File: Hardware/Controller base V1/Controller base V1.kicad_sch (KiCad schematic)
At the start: 30 parts, among them J1 USB_C_Receptacle_USB2.0_16P, J2 Conn_01x05_Pin, J7 Conn_02x10_Counter_Clockwise, J8 Conn_02x10_Counter_Clockwise, SW4 SW_Push, U1 AZ1117CH-3.3TRG1, U2 ESP32-S3-WROOM-1U-N4

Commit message: update
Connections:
- net GND: no longer J8.16, J8.18
- net GPIO39: now reaches U2.32 (IO39)
- net GPIO39: now also J8.16
- net GPIO40: now reaches U2.33 (IO40)
- net GPIO40: now also J8.18
- no-connect marks 6 -> 4
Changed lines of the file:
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@@
 	)
 	(junction
-		(at 271.78 91.44)
-		(diameter 0)
-		(color 0 0 0 0)
-	)
-	(junction
 		(at 157.48 31.75)
 		(diameter 0)
@@
 	)
 	(no_connect
-		(at 209.55 127)
-	)
-	(no_connect
 		(at 48.26 64.77)
 	)
 	(no_connect
-		(at 209.55 129.54)
-	)
-	(no_connect
 		(at 48.26 62.23)
 	)
@@
 	(wire
 		(pts
-			(xy 21.59 163.83) (xy 29.21 163.83)
+			(xy 271.78 97.79) (xy 271.78 93.98)
 		)
 		(stroke
@@
 	(wire
 		(pts
-			(xy 102.87 31.75) (xy 115.57 31.75)
+			(xy 209.55 127) (xy 210.82 127)
 		)
 		(stroke
@@
 	(wire
 		(pts
-			(xy 210.82 132.08) (xy 209.55 132.08)
+			(xy 21.59 163.83) (xy 29.21 163.83)
 		)
 		(stroke
@@
 	(wire
 		(pts
-			(xy 154.94 152.4) (xy 154.94 144.78)
+			(xy 102.87 31.75) (xy 115.57 31.75)
 		)
 		(stroke
@@
 	(wire
 		(pts
-			(xy 176.53 134.62) (xy 179.07 134.62)
+			(xy 210.82 132.08) (xy 209.55 132.08)
 		)
 		(stroke
@@
 	(wire
 		(pts
-			(xy 81.28 189.23) (xy 87.63 189.23)
+			(xy 154.94 152.4) (xy 154.94 144.78)
 		)
 		(stroke
@@
 	(wire
 		(pts
-			(xy 271.78 88.9) (xy 271.78 91.44)
+			(xy 176.53 134.62) (xy 179.07 134.62)
+		)
+		(stroke
+			(width 0)
+			(type default)
+		)
+	)
+	(wire
+		(pts
+			(xy 81.28 189.23) (xy 87.63 189.23)
 		)
 		(stroke
@@
 	(wire
 		(pts
-			(xy 271.78 91.44) (xy 276.86 91.44)
-		)
-		(stroke
-			(width 0)
-			(type default)
-		)
-	)
-	(wire
-		(pts
 			(xy 247.65 83.82) (xy 252.73 83.82)
 		)
@@
 	(wire
 		(pts
+			(xy 209.55 129.54) (xy 210.82 129.54)
+		)
+		(stroke
+			(width 0)
+			(type default)
+		)
+	)
+	(wire
+		(pts
 			(xy 153.67 87.63) (xy 153.67 88.9)
 		)
@@
 	(wire
 		(pts
-			(xy 271.78 93.98) (xy 271.78 91.44)
-		)
-		(stroke
-			(width 0)
-			(type default)
-		)
-	)
-	(wire
-		(pts
 			(xy 170.18 31.75) (xy 170.18 34.29)
 		)
@@
 	(wire
 		(pts
-			(xy 265.43 88.9) (xy 271.78 88.9)
+			(xy 247.65 76.2) (xy 252.73 76.2)
 		)
 		(stroke
@@
 	(wire
 		(pts
-			(xy 247.65 76.2) (xy 252.73 76.2)
+			(xy 210.82 144.78) (xy 209.55 144.78)
 		)
 		(stroke
@@
 	(wire
 		(pts
-			(xy 210.82 144.78) (xy 209.55 144.78)
+			(xy 67.31 49.53) (xy 67.31 57.15)
 		)
 		(stroke
@@
 	(wire
 		(pts
-			(xy 67.31 49.53) (xy 67.31 57.15)
+			(xy 55.88 85.09) (xy 49.53 85.09)
 		)
 		(stroke
@@
 	(wire
 		(pts
-			(xy 55.88 85.09) (xy 49.53 85.09)
+			(xy 271.78 59.69) (xy 271.78 57.15)
 		)
 		(stroke
@@
 	(wire
 		(pts
-			(xy 271.78 59.69) (xy 271.78 57.15)
+			(xy 74.93 52.07) (xy 72.39 52.07)
 		)
 		(stroke
@@
 	(wire
 		(pts
-			(xy 74.93 52.07) (xy 72.39 52.07)
+			(xy 67.31 46.99) (xy 48.26 46.99)
 		)
 		(stroke
@@
 	(wire
 		(pts
-			(xy 67.31 46.99) (xy 48.26 46.99)
+			(xy 265.43 91.44) (xy 271.78 91.44)
 		)
 		(stroke
@@
 	(wire
 		(pts
-			(xy 59.69 34.29) (xy 59.69 57.15)
+			(xy 265.43 88.9) (xy 271.78 88.9)
 		)
 		(stroke
@@
 	(wire
 		(pts
-			(xy 271.78 54.61) (xy 271.78 52.07)
+			(xy 59.69 34.29) (xy 59.69 57.15)
 		)
 		(stroke
@@
 	(wire
 		(pts
-			(xy 53.34 80.01) (xy 49.53 80.01)
+			(xy 271.78 54.61) (xy 271.78 52.07)
 		)
 		(stroke
@@
 	(wire
 		(pts
-			(xy 49.53 179.07) (xy 58.42 179.07)
+			(xy 53.34 80.01) (xy 49.53 80.01)
 		)
 		(stroke
@@
 	(wire
 		(pts
-			(xy 81.28 186.69) (xy 87.63 186.69)
+			(xy 49.53 179.07) (xy 58.42 179.07)
 		)
 		(stroke
@@
 	(wire
 		(pts
-			(xy 132.08 41.91) (xy 132.08 46.99)
+			(xy 81.28 186.69) (xy 87.63 186.69)
 		)
 		(stroke
@@
 	(wire
 		(pts
-			(xy 265.43 91.44) (xy 271.78 91.44)
+			(xy 132.08 41.91) (xy 132.08 46.99)
 		)
 		(stroke
@@
 		)
 	)
+	(global_label "GPIO40"
+		(shape input)
+		(at 271.78 91.44 0)
+		(fields_autoplaced yes)
+		(effects
+			(font
+				(size 1.27 1.27)
+			)
+			(justify left)
+		)
+		(property "Intersheetrefs" "${INTERSHEET_REFS}"
+			(at 281.6595 91.44 0)
+			(effects
+				(font
+					(size 1.27 1.27)
+				)
+				(justify left)
+				(hide yes)
+			)
+		)
+	)
 	(global_label "GPIO11"
 		(shape input)
@@
 		)
 	)
+	(global_label "GPIO39"
+		(shape input)
+		(at 210.82 127 0)
+		(fields_autoplaced yes)
+		(effects
+			(font
+				(size 1.27 1.27)
+			)
+			(justify left)
+		)
+		(property "Intersheetrefs" "${INTERSHEET_REFS}"
+			(at 220.6995 127 0)
+			(effects
+				(font
+					(size 1.27 1.27)
+				)
+				(justify left)
+				(hide yes)
+			)
+		)
+	)
 	(global_label "GPIO4"
 		(shape input)
@@
 		)
 	)
+	(global_label "GPIO39"
+		(shape input)
+		(at 271.78 88.9 0)
+		(fields_autoplaced yes)
+		(effects
+			(font
+				(size 1.27 1.27)
+			)
+			(justify left)
+		)
+		(property "Intersheetrefs" "${INTERSHEET_REFS}"
+			(at 281.6595 88.9 0)
+			(effects
+				(font
+					(size 1.27 1.27)
+				)
+				(justify left)
+				(hide yes)
+			)
+		)
+	)
 	(global_label "GPIO8"
 		(shape input)
@@
 		)
 	)
+	(global_label "GPIO40"
+		(shape input)
+		(at 210.82 129.54 0)
+		(fields_autoplaced yes)
+		(effects
+			(font
+				(size 1.27 1.27)
+			)
+			(justify left)
+		)
+		(property "Intersheetrefs" "${INTERSHEET_REFS}"
+			(at 220.6995 129.54 0)
+			(effects
+				(font
+					(size 1.27 1.27)
+				)
+				(justify left)
+				(hide yes)
+			)
+		)
+	)
 	(global_label "GPIO38"
 		(shape input)
@@
 	(symbol
 		(lib_id "MCU_Controller:GND")
-		(at 276.86 91.44 90)
+		(at 271.78 97.79 0)
 		(unit 1)
 		(exclude_from_sim no)
@@
 		(fields_autoplaced yes)
 		(property "Reference" "#PWR030"
-			(at 283.21 91.44 0)
+			(at 271.78 104.14 0)
 			(effects
 				(font
@@
 		)
 		(property "Value" "GND"
-			(at 280.67 91.4399 90)
+			(at 274.32 99.0599 0)
 			(effects
 				(font
 					(size 1.27 1.27)
 				)
-				(justify right)
+				(justify left)
 			)
 		)
 		(property "Footprint" ""
-			(at 276.86 91.44 0)
+			(at 271.78 97.79 0)
 			(effects
 				(font
@@
 		)
 		(property "Datasheet" ""
-			(at 276.86 91.44 0)
+			(at 271.78 97.79 0)
 			(effects
 				(font
@@
 		)
 		(property "Description" "Power symbol creates a global label with name \"GND\" , ground"
-			(at 276.86 91.44 0)
+			(at 271.78 97.79 0)
 			(effects
 				(font

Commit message: added test points
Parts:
- added 3V3, Gnd1, VBUS1: TestPoint, MCU_Controller:TestPoint_Pad_D1.0mm, symbol MCU_Controller:TestPoint
- renumbered TP4 to D+1, TP3 to D-1, J7 to J3, J8 to J4, TP1 to RX0, SW4 to SW1, TP2 to TX0
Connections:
- net GND: now also Gnd1.1
- net VBUS: now also VBUS1.1
- net VCC_3V3: now also 3V3.1

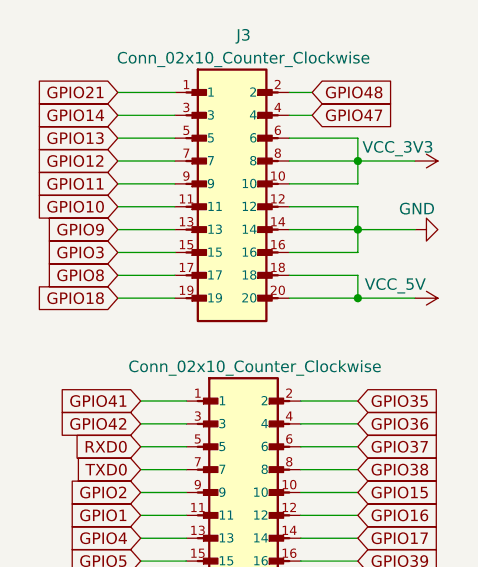
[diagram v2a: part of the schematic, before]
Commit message: updated power trace for expansion
made where there is 5v to carrier board for future batter expansion
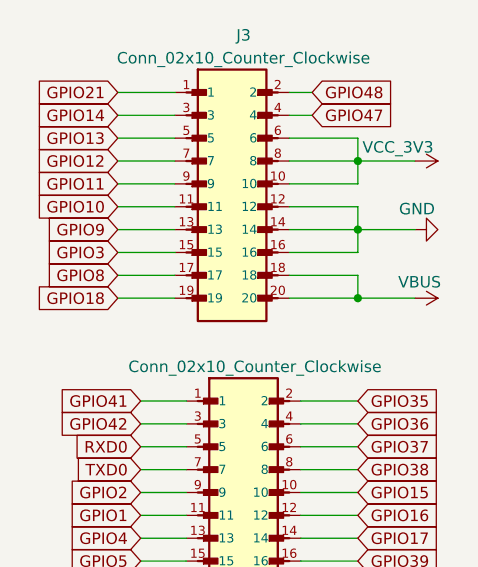
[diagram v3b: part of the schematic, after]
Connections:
- net VBUS: now also J3.18, J3.20
- net VCC_5V: no longer J3.18, J3.20
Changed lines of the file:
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@@
-	)
-	(symbol
-		(lib_id "MCU_Controller:+5V")
-		(at 278.13 59.69 270)
-		(unit 1)
-		(exclude_from_sim no)
-		(in_bom yes)
-		(on_board yes)
-		(dnp no)
-		(property "Reference" "#PWR022"
-			(at 274.32 59.69 0)
-			(effects
-				(font
-					(size 1.27 1.27)
-				)
-				(hide yes)
-			)
-		)
-		(property "Value" "VCC_5V"
-			(at 272.542 58.166 90)
-			(effects
-				(font
-					(size 1.27 1.27)
-				)
-				(justify left)
-			)
-		)
-		(property "Footprint" ""
-			(at 278.13 59.69 0)
-			(effects
-				(font
-					(size 1.27 1.27)
-				)
-				(hide yes)
-			)
-		)
-		(property "Datasheet" ""
-			(at 278.13 59.69 0)
-			(effects
-				(font
-					(size 1.27 1.27)
-				)
-				(hide yes)
-			)
-		)
-		(property "Description" "Power symbol creates a global label with name \"+5V\""
-			(at 278.13 59.69 0)
-			(effects
-				(font
-					(size 1.27 1.27)
-				)
-				(hide yes)
-			)
-		)
-		(pin "1"
-		)
-		(instances
-			(project "Controller base V0.5"
-				(path "/5ff5287b-60c7-4258-8bdb-42f045207b2d"
-					(reference "#PWR022")
-					(unit 1)
-				)
-			)
-		)
 	)
 	(symbol
@@
 					(unit 1)
 				)
+			)
+		)
+	)
+	(symbol
+		(lib_id "MCU_Controller:VBUS")
+		(at 278.13 59.69 270)
+		(unit 1)
+		(exclude_from_sim no)
+		(in_bom yes)
+		(on_board yes)
+		(dnp no)
+		(property "Reference" "#PWR022"
+			(at 274.32 59.69 0)
+			(effects
+				(font
+					(size 1.27 1.27)
+				)
+				(hide yes)
+			)
+		)
+		(property "Value" "VBUS"
+			(at 278.638 57.912 90)
+			(effects
+				(font
+					(size 1.27 1.27)
+				)
+			)
+		)
+		(property "Footprint" ""
+			(at 278.13 59.69 0)
+			(effects
+				(font
+					(size 1.27 1.27)
+				)
+				(hide yes)
+			)
+		)
+		(property "Datasheet" ""
+			(at 278.13 59.69 0)
+			(effects
+				(font
+					(size 1.27 1.27)
+				)
+				(hide yes)
+			)
+		)
+		(property "Description" "Power symbol creates a global label with name \"VBUS\""
+			(at 278.13 59.69 0)
+			(effects
+				(font
+					(size 1.27 1.27)
+				)
+				(hide yes)
+			)
+		)
+		(pin "1"
+		)
+		(instances
+			(project "Controller base V1"
+				(path "/5ff5287b-60c7-4258-8bdb-42f045207b2d"
+					(reference "#PWR022")
+					(unit 1)
+				)
